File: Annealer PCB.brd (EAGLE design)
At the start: 53.3 x 77.5 mm, 42 parts, among them T1-BYPASS JUMPER-SMT_3_1-NC_TRACE_SILK, T2-BYPASS JUMPER-SMT_3_1-NC_TRACE_SILK

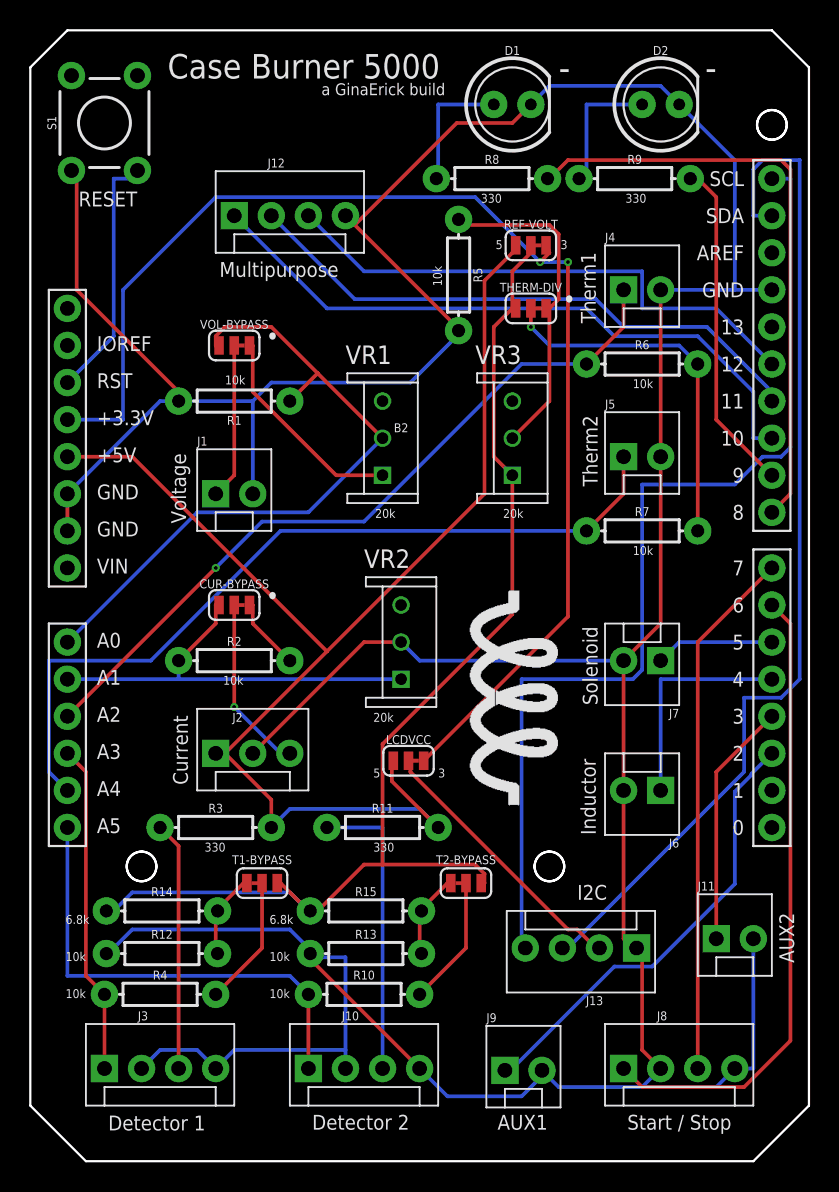
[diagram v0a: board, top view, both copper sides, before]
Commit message: Fixed hole sizes and moved things accordingly
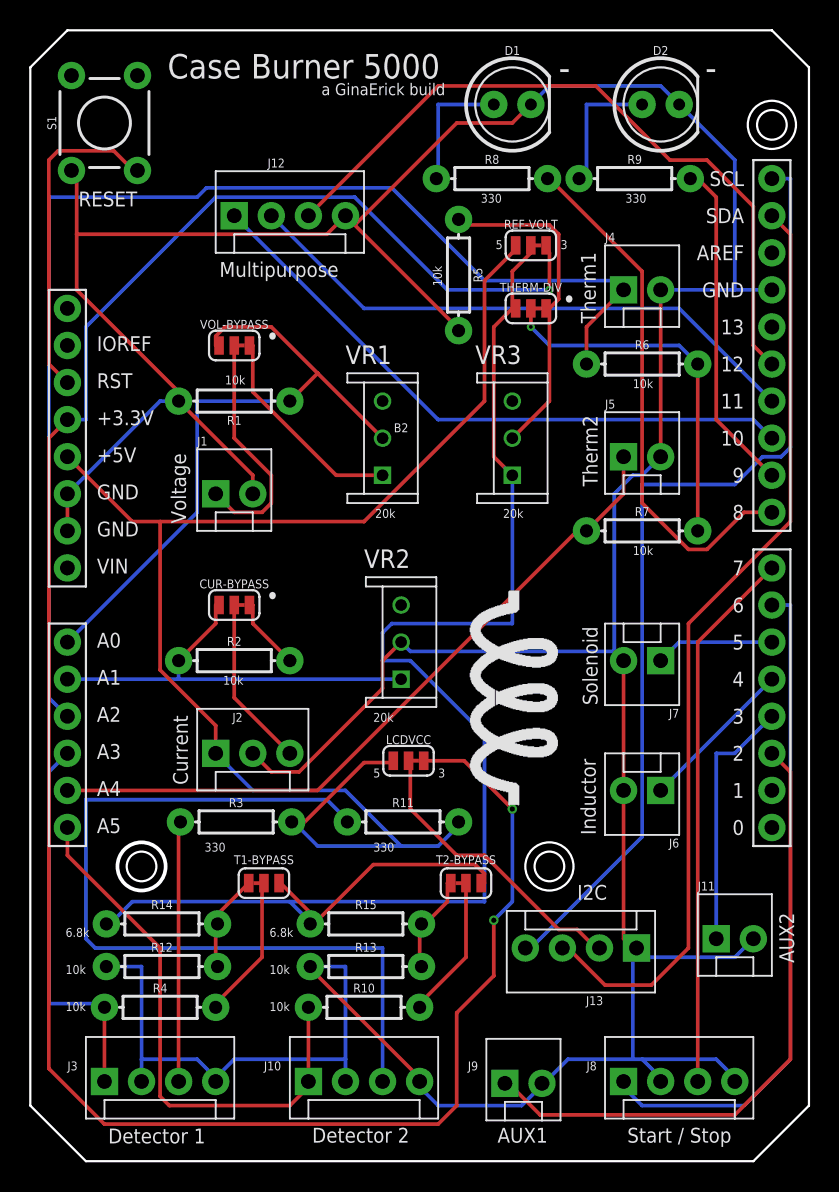
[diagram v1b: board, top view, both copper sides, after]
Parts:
- moved R11 1.45 mm to (34.4, 25.8)
- moved R3 1.45 mm to (23.0, 25.8)
- moved J10 0.89 mm to (27.9, 8.00)
- moved J3 0.89 mm to (14.0, 8.00)
- moved J8 0.89 mm to (49.5, 8.00)
- moved R10 0.89 mm to (31.8, 13.1)
- moved R4 0.89 mm to (17.8, 13.1)
- moved J9 0.89 mm to (41.4, 7.87)
- moved R12 0.89 mm to (17.9, 15.9)
- moved R13 0.89 mm to (31.9, 15.9)
- moved R14 0.89 mm to (17.9, 18.8)
- moved R15 0.89 mm to (31.9, 18.8)
- moved T1-BYPASS 0.13 mm to (24.9, 21.6)
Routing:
- net 3.3V: track 87.4 -> 153.1 mm, vias 2 -> 3
- net N$6: track 20.3 -> 57.8 mm
- net A2: track 51.7 -> 84.7 mm, vias 1 -> 0
- net VREF: track 80.4 -> 106.3 mm
- net D2: track 31.0 -> 43.5 mm
- net D12: track 37.4 -> 48.9 mm
- net 5V: track 91.7 -> 100.0 mm
- net A4: track 56.1 -> 49.1 mm
- net SDA: track 70.3 -> 64.3 mm
- net N$5: track 10.7 -> 16.4 mm
- net RESET: track 17.2 -> 22.6 mm
- net D8: track 41.4 -> 36.2 mm
- net A5: track 32.3 -> 37.5 mm
- net GND: track 292.2 -> 287.6 mm
- net SCL: track 70.8 -> 66.2 mm
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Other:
- outline, holes or cut-outs redrawn

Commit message: v4 board update
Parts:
- removed R10, R12, R13, R4: 10k, SparkFun-Resistors:AXIAL-0.3
- removed R11, R3: 330, SparkFun-Resistors:AXIAL-0.3
- removed R14, R15: 6800, SparkFun-Resistors:AXIAL-0.3
- removed T1-BYPASS, T2-BYPASS: JUMPER-SMT_3_1-NC_TRACE_SILK, SparkFun-Jumpers:SMT-JUMPER_3_1-NC_TRACE_SILK
- J10, J3: value (none) -> CONN_5X1_MOLEX_POLAR; device SparkFun-Connectors:MOLEX-1X4 -> dave-connectors:MOLEX-5
- moved R5 42.3 mm to (52.5, 23.4), turned to 0 degrees
- moved REF-VOLT 37.1 mm to (35.1, 29.1)
- moved J13 36.6 mm to (13.8, 16.4), turned to 0 degrees
- moved J11 34.4 mm to (23.0, 7.87)
- moved J3 31.8 mm to (45.7, 7.62)
- moved J9 27.3 mm to (14.1, 7.87)
- moved J6 26.8 mm to (27.9, 16.4), turned to 0 degrees
- moved J7 25.5 mm to (36.8, 16.4), turned to 0 degrees
- moved VR3 22.2 mm to (50.8, 31.8)
- moved THERM-DIV 22.1 mm to (50.3, 40.0)
- moved J10 19.7 mm to (45.7, 16.5)
- moved J8 18.2 mm to (31.4, 7.87)
- moved LCDVCC 5.72 mm to (35.1, 24.3)
- moved R7 1.37 mm to (50.0, 44.6)
- moved J12 1.27 mm to (22.9, 68.6)
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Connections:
- removed net N$1: R4.P$2, T1-BYPASS.2
- removed net N$11: R12.P$2, R14.P$2, T1-BYPASS.3
- removed net N$13: R13.P$2, R15.P$2, T2-BYPASS.3
- removed net N$15: J3.3, R3.P$1
- removed net N$6: J10.3, R11.P$1
- removed net N$8: R10.P$2, T2-BYPASS.2
- net 5V: now also J10.4, J3.4; no longer R11.P$2, R3.P$2
- net A3: no longer R4.P$1
- net A5: no longer R10.P$1
- net D2: now also J8.3; no longer J9.1
- net D3: now also J8.1; no longer J11.1
- net D6: now also J9.1; no longer J8.1
- net D7: now also J11.1; no longer J8.3
- net GND: now also J10.3, J10.5, J3.3, J3.5; no longer J10.2, J10.4, J3.2, J3.4, R12.P$1, R13.P$1
- net VREF: now also J10.2, J3.2; no longer R14.P$1, R15.P$1, T1-BYPASS.1, T2-BYPASS.1
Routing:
- net GND: track 287.6 -> 16.4 mm
- net 3.3V: track 153.1 -> 63.4 mm, vias 3 -> 1
- net N$6: track 57.8 -> 0.00 mm
- net VREF: track 106.3 -> 56.9 mm
- net SCL: track 66.2 -> 111.2 mm
- net D5: track 8.15 -> 45.5 mm
- net D6: track 46.0 -> 81.1 mm
- net A2: track 84.7 -> 51.4 mm
- net A3: track 26.8 -> 59.3 mm
- net D3: track 17.6 -> 47.3 mm
- net D4: track 10.8 -> 39.8 mm
- net N$15: track 17.8 -> 0.00 mm
- net D7: track 37.3 -> 55.0 mm
- net N$2: track 11.7 -> 28.0 mm
- net D12: track 48.9 -> 36.5 mm
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- added copper zone on layer 1, net GND
- added copper zone on layer 16, net GND
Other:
- board text added: "Encoder"
- board text added: "Version 4.0"
- board text removed: "6.8k"
- board text removed: "Multipurpose"
- board text removed: "Version 3.2"

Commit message: 4.1 - add power-on LED
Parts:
- added J14: (no value), SparkFun-Connectors:MOLEX-1X2
- added R3: 330, SparkFun-Resistors:AXIAL-0.3
- moved J12 13.1 mm to (34.3, 62.2)
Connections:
- new net N$1: J14.1, R3.P$1
- net 5V: now also R3.P$2
- net GND: now also J14.2
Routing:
- net 5V: track 89.3 -> 113.1 mm
- net D10: track 47.0 -> 33.0 mm
- net D12: track 36.5 -> 24.0 mm
- net D11: track 40.8 -> 30.4 mm, vias 0 -> 1
- net N$1: track 0.00 -> 8.67 mm
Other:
- board text added: "Version 4.1"
- board text removed: "Version 4.0"
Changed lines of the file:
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@@
 <text x="13.716" y="3.683" size="1.016" layer="21">AUX1</text>
 <text x="22.606" y="3.683" size="1.016" layer="21">AUX2</text>
-<text x="24.13" y="64.262" size="1.016" layer="21">Encoder</text>
-<text x="21.59" y="66.929" size="1.778" layer="22" rot="MR0">+</text>
+<text x="35.56" y="57.912" size="1.016" layer="21">Encoder</text>
+<text x="33.02" y="60.579" size="1.778" layer="22" rot="MR0">+</text>
 <rectangle x1="44.7802" y1="31.1658" x2="45.2374" y2="31.2166" layer="21" rot="R90"/>
 <rectangle x1="44.7802" y1="34.2646" x2="45.2374" y2="34.3154" layer="21" rot="R90"/>
@@
 <text x="44.45" y="14.478" size="1.778" layer="22" rot="MR0">+</text>
 <text x="44.45" y="5.842" size="1.778" layer="22" rot="MR0">+</text>
-<text x="39.116" y="44.196" size="0.8128" layer="22" rot="MR0">Version 4.0</text>
+<text x="39.116" y="44.196" size="0.8128" layer="22" rot="MR0">Version 4.1</text>
 <text x="22.225" y="55.753" size="0.6096" layer="21">10k</text>
 <text x="49.403" y="42.672" size="0.6096" layer="21">10k</text>
@@
 <attribute name="VALUE" x="21.717" y="5.08" size="0.6096" layer="27" font="vector" ratio="20" align="top-left"/>
 </element>
-<element name="J12" library="SparkFun-Connectors" package="MOLEX-1X4" value="" x="22.86" y="68.58" smashed="yes">
-<attribute name="NAME" x="25.146" y="71.882" size="0.6096" layer="25" font="vector" ratio="20"/>
-<attribute name="PROD_ID" value="CONN-08186" x="22.86" y="68.58" size="1.778" layer="27" display="off"/>
-<attribute name="SF_ID" value="PRT-08231" x="22.86" y="68.58" size="1.778" layer="27" display="off"/>
-<attribute name="VALUE" x="25.146" y="65.151" size="0.6096" layer="27" font="vector" ratio="20"/>
+<element name="J12" library="SparkFun-Connectors" package="MOLEX-1X4" value="" x="34.29" y="62.23" smashed="yes">
+<attribute name="NAME" x="36.576" y="65.532" size="0.6096" layer="25" font="vector" ratio="20"/>
+<attribute name="PROD_ID" value="CONN-08186" x="34.29" y="62.23" size="1.778" layer="27" display="off"/>
+<attribute name="SF_ID" value="PRT-08231" x="34.29" y="62.23" size="1.778" layer="27" display="off"/>
+<attribute name="VALUE" x="36.576" y="58.801" size="0.6096" layer="27" font="vector" ratio="20"/>
 </element>
 <element name="J13" library="SparkFun-Connectors" package="MOLEX-1X4" value="" x="13.843" y="16.383" smashed="yes">
@@
 <element name="J3" library="dave-connectors" package="MOLEX-5" value="CONN_5X1_MOLEX_POLAR" x="45.72" y="7.62" smashed="yes"/>
 <element name="J10" library="dave-connectors" package="MOLEX-5" value="CONN_5X1_MOLEX_POLAR" x="45.72" y="16.51" smashed="yes"/>
+<element name="J14" library="SparkFun-Connectors" package="MOLEX-1X2" value="" x="21.59" y="68.58" smashed="yes">
+<attribute name="NAME" x="20.32" y="71.882" size="0.6096" layer="25" font="vector" ratio="20"/>
+<attribute name="SF_ID" value="PRT-09918" x="21.59" y="68.58" size="1.778" layer="27" display="off"/>
+<attribute name="VALUE" x="20.32" y="65.786" size="0.6096" layer="27" font="vector" ratio="20" align="top-left"/>
+</element>
+<element name="R3" library="SparkFun-Resistors" package="AXIAL-0.3" value="330" x="27.94" y="68.58" smashed="yes" rot="R270">
+<attribute name="NAME" x="28.956" y="68.58" size="0.6096" layer="25" font="vector" ratio="20" rot="R270" align="bottom-center"/>
+<attribute name="PROD_ID" value="RES-8371" x="27.94" y="68.58" size="1.778" layer="27" rot="R270" display="off"/>
+<attribute name="VALUE" x="26.924" y="68.58" size="0.6096" layer="27" font="vector" ratio="20" rot="R270" align="top-center"/>
+</element>
 </elements>
 <signals>
@@
 <vertex x="8.89" y="6.35"/>
 </polygon>
+<contactref element="J14" pad="2"/>
 </signal>
 <signal name="3.3V">
@@
 <wire x1="33.02" y1="29.21" x2="33.02" y2="20.32" width="0.254" layer="1"/>
 <via x="33.02" y="20.32" extent="1-16" drill="0.254"/>
+<contactref element="R3" pad="P$2"/>
+<wire x1="11.43" y1="50.8" x2="17.78" y2="57.15" width="0.254" layer="1"/>
+<wire x1="17.78" y1="57.15" x2="17.78" y2="59.69" width="0.254" layer="1"/>
+<wire x1="17.78" y1="59.69" x2="22.86" y2="64.77" width="0.254" layer="1"/>
+<wire x1="22.86" y1="64.77" x2="27.94" y2="64.77" width="0.254" layer="1"/>
 </signal>
 <signal name="RESET">
@@
 <contactref element="B2" pad="D10"/>
 <contactref element="J12" pad="1"/>
-<wire x1="35.56" y1="55.88" x2="22.86" y2="68.58" width="0.254" layer="1"/>
-<wire x1="50.165" y1="55.88" x2="35.56" y2="55.88" width="0.254" layer="1"/>
+<wire x1="40.64" y1="55.88" x2="34.29" y2="62.23" width="0.254" layer="1"/>
+<wire x1="50.165" y1="55.88" x2="40.64" y2="55.88" width="0.254" layer="1"/>
 <wire x1="53.34" y1="59.055" x2="50.165" y2="55.88" width="0.254" layer="1"/>
 <wire x1="53.975" y1="59.055" x2="53.34" y2="59.055" width="0.254" layer="1"/>
@@
 <contactref element="B2" pad="D11"/>
 <contactref element="J12" pad="2"/>
-<wire x1="30.48" y1="63.5" x2="25.4" y2="68.58" width="0.254" layer="1"/>
-<wire x1="52.07" y1="63.5" x2="30.48" y2="63.5" width="0.254" layer="1"/>
-<wire x1="58.42" y1="57.15" x2="52.07" y2="63.5" width="0.254" layer="1"/>
-<wire x1="58.42" y1="55.88" x2="58.42" y2="57.15" width="0.254" layer="1"/>
-<wire x1="59.69" y1="54.61" x2="58.42" y2="55.88" width="0.254" layer="1"/>
+<wire x1="39.37" y1="64.77" x2="36.83" y2="62.23" width="0.254" layer="1"/>
+<wire x1="53.34" y1="64.77" x2="39.37" y2="64.77" width="0.254" layer="1"/>
+<wire x1="57.15" y1="60.96" x2="53.34" y2="64.77" width="0.254" layer="1"/>
+<via x="57.15" y="60.96" extent="1-16" drill="0.35"/>
+<wire x1="57.15" y1="60.96" x2="57.15" y2="57.15" width="0.254" layer="16"/>
+<wire x1="57.15" y1="57.15" x2="59.69" y2="54.61" width="0.254" layer="16"/>
 </signal>
 <signal name="D12">
 <contactref element="B2" pad="D12"/>
 <contactref element="J12" pad="3"/>
-<wire x1="32.385" y1="64.135" x2="27.94" y2="68.58" width="0.254" layer="1"/>
-<wire x1="52.705" y1="64.135" x2="32.385" y2="64.135" width="0.254" layer="1"/>
+<wire x1="41.275" y1="64.135" x2="39.37" y2="62.23" width="0.254" layer="1"/>
+<wire x1="52.705" y1="64.135" x2="41.275" y2="64.135" width="0.254" layer="1"/>
 <wire x1="59.69" y1="57.15" x2="52.705" y2="64.135" width="0.254" layer="1"/>
 </signal>
@@
 <wire x1="50.8" y1="29.21" x2="50.8" y2="23.495" width="0.254" layer="1"/>
 </signal>
+<signal name="N$1">
+<contactref element="R3" pad="P$1"/>
+<contactref element="J14" pad="1"/>
+<wire x1="27.94" y1="72.39" x2="26.67" y2="71.12" width="0.254" layer="1"/>
+<wire x1="26.67" y1="71.12" x2="22.86" y2="71.12" width="0.254" layer="1"/>
+<wire x1="22.86" y1="71.12" x2="21.59" y2="69.85" width="0.254" layer="1"/>
+<wire x1="21.59" y1="69.85" x2="21.59" y2="68.58" width="0.254" layer="1"/>
+</signal>
 </signals>
